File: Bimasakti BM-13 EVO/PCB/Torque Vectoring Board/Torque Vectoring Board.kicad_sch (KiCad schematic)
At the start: 24 parts, among them J1 +5, J2 Can ESC 1, J3 Can ESC 2, J4 APPS, J5 +12, J6 Steering Angle, J7 GPOS, U3 SN65HVD230, U4 SN65HVD230, U5 ADS1115IDGS

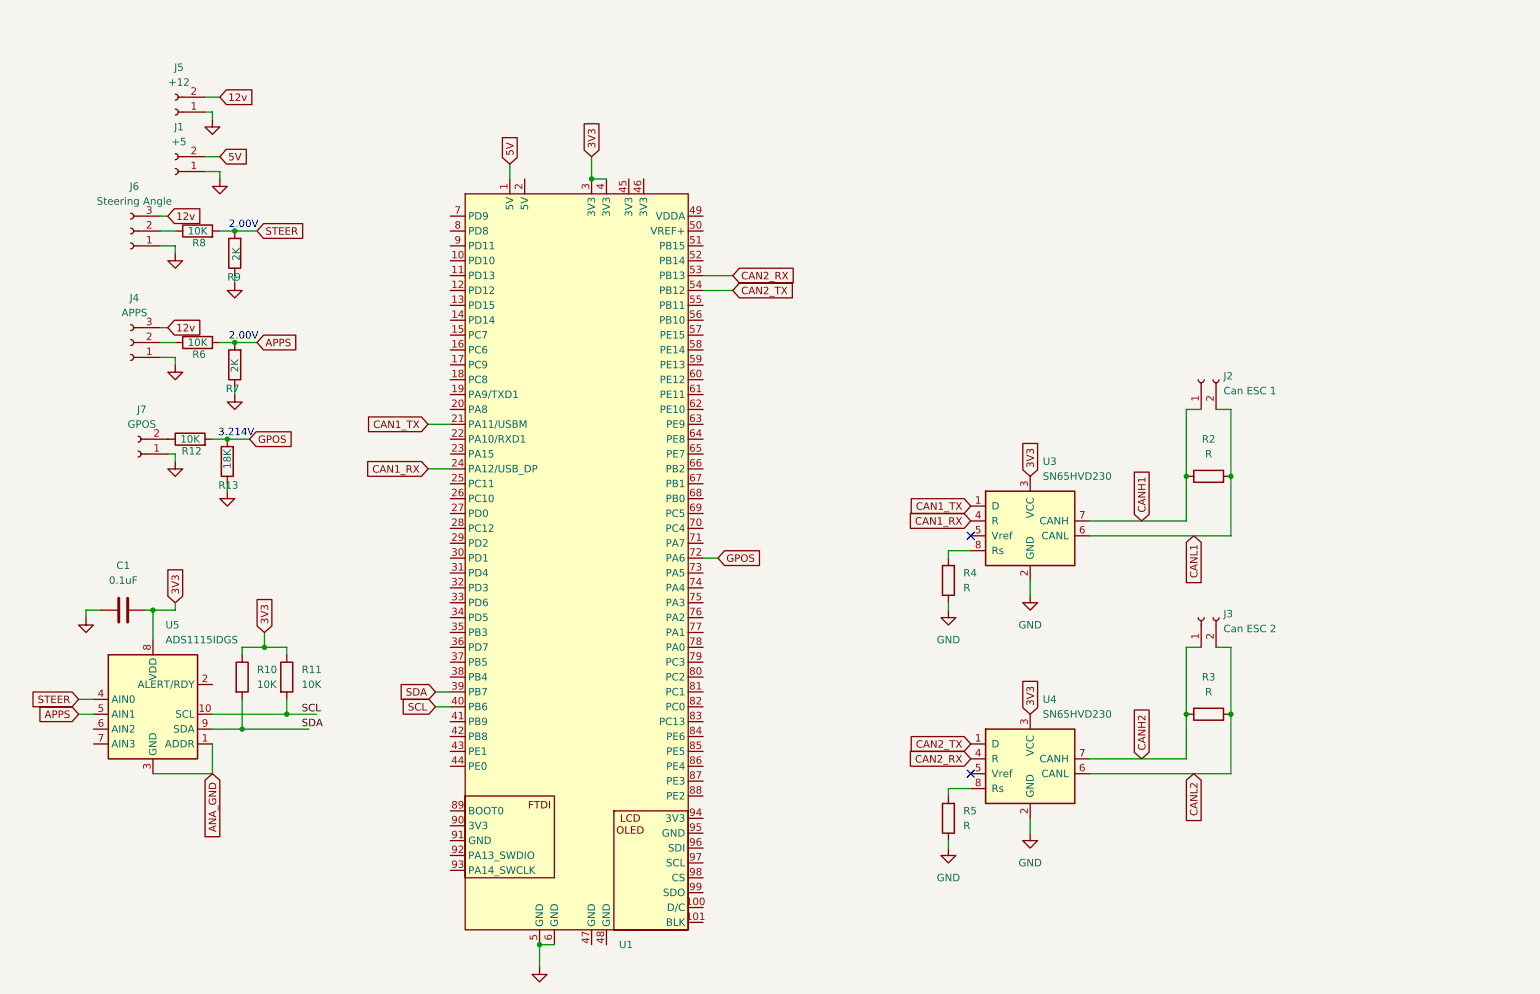
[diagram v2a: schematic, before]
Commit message: tv board kurang IMU
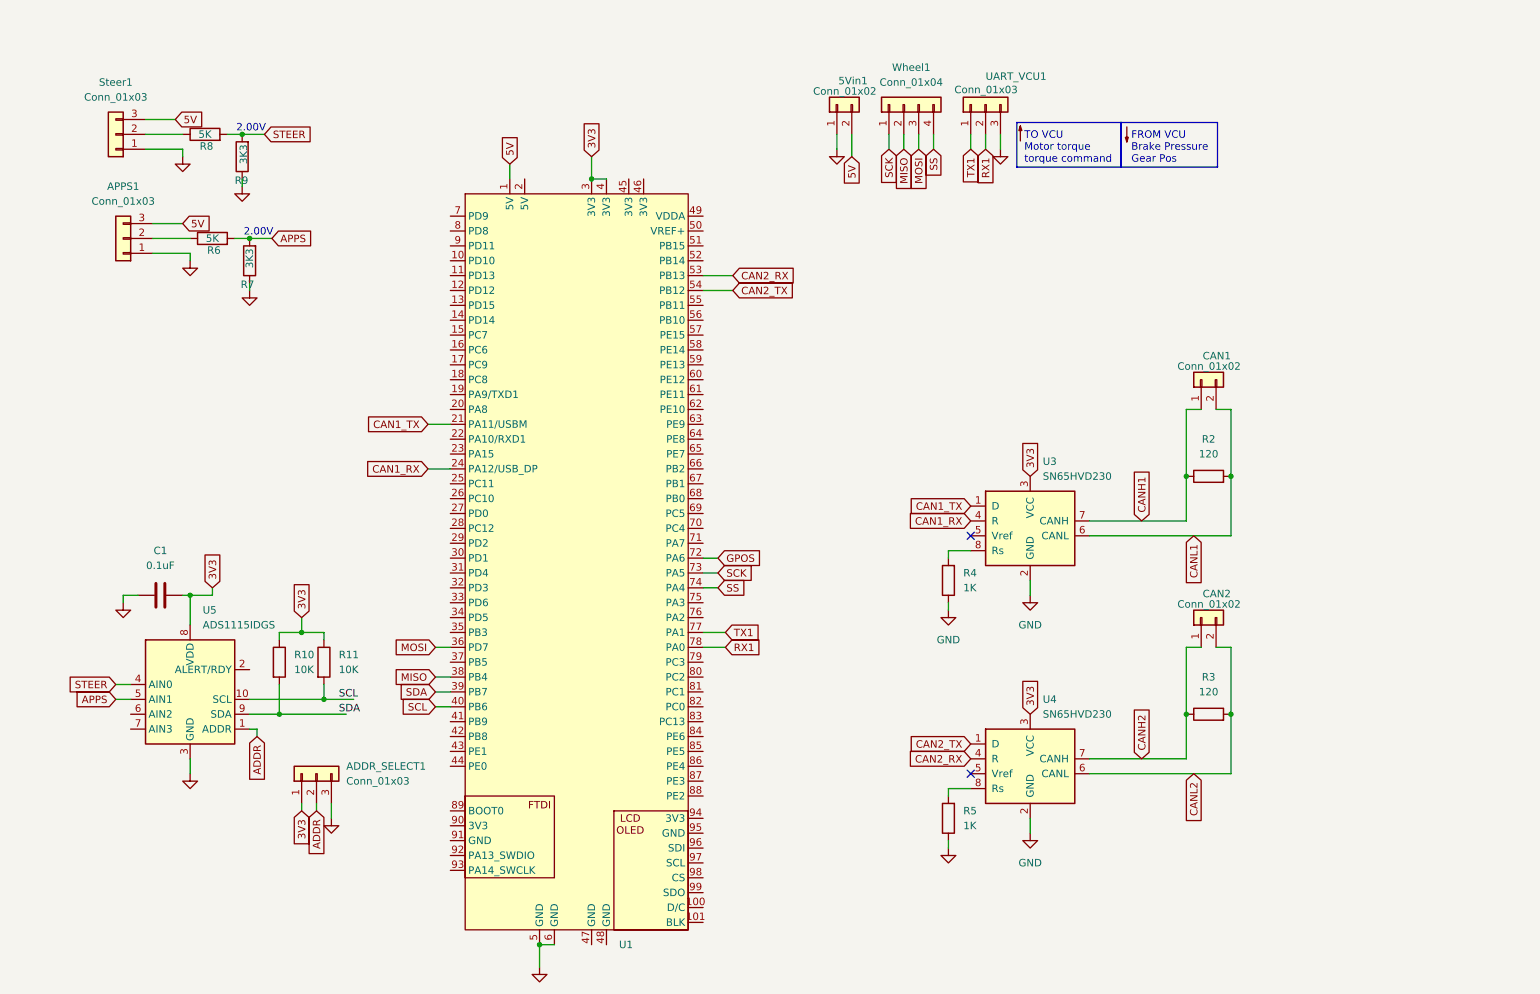
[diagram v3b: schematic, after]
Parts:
- removed J1: +5, Connector_JST:JST_EH_B2B-EH-A_1x02_P2.50mm_Vertical, symbol Connector:Conn_01x02_Socket
- removed J2: Can ESC 1, Connector_JST:JST_EH_B2B-EH-A_1x02_P2.50mm_Vertical, symbol Connector:Conn_01x02_Socket
- removed J3: Can ESC 2, Connector_JST:JST_EH_B2B-EH-A_1x02_P2.50mm_Vertical, symbol Connector:Conn_01x02_Socket
- removed J4: APPS, symbol Connector:Conn_01x03_Socket
- removed J5: +12, Connector_JST:JST_EH_B2B-EH-A_1x02_P2.50mm_Vertical, symbol Connector:Conn_01x02_Socket
- removed J6: Steering Angle, symbol Connector:Conn_01x03_Socket
- removed J7: GPOS, symbol Connector:Conn_01x02_Socket
- removed R12: 10K, Resistor_SMD:R_0805_2012Metric, symbol Device:R
- removed R13: 18K, Resistor_SMD:R_0805_2012Metric, symbol Device:R
- added 5Vin1, CAN1, CAN2: Conn_01x02, Connector_JST:JST_XH_B2B-XH-A_1x02_P2.50mm_Vertical, symbol Connector_Generic:Conn_01x02
- added ADDR_SELECT1: Conn_01x03, Connector_PinHeader_2.54mm:PinHeader_1x03_P2.54mm_Vertical, symbol Connector_Generic:Conn_01x03
- added APPS1, Steer1, UART_VCU1: Conn_01x03, Connector_JST:JST_XH_B3B-XH-A_1x03_P2.50mm_Vertical, symbol Connector_Generic:Conn_01x03
- added Wheel1: Conn_01x04, Connector_JST:JST_XH_B4B-XH-A_1x04_P2.50mm_Vertical, symbol Connector_Generic:Conn_01x04
- R2, R3: value R -> 120
- R4, R5: value R -> 1K
- R6, R8: value 10K -> 5K
- R7, R9: value 2K -> 3K3
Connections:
- net 3V3: now also ADDR_SELECT1.1 (Pin_1)
- net 5V: now also 5Vin1.2 (Pin_2), APPS1.3 (Pin_3), Steer1.3 (Pin_3)
- net CANH1: now also CAN1.1 (Pin_1)
- net CANH2: now also CAN2.1 (Pin_1)
- net CANL1: now also CAN1.2 (Pin_2)
- net CANL2: now also CAN2.2 (Pin_2)
- net GND: now also U5.3 (GND), 5Vin1.1 (Pin_1), ADDR_SELECT1.3 (Pin_3), APPS1.1 (Pin_1), Steer1.1 (Pin_1), UART_VCU1.3 (Pin_3)
- net at R8.1: now also Steer1.2 (Pin_2)
- net at R6.1: now also APPS1.2 (Pin_2)
- net MOSI: now reaches U1.36 (PD7)
- net MOSI: now also Wheel1.3 (Pin_3)
- net MISO: now reaches U1.38 (PB4)
- net MISO: now also Wheel1.2 (Pin_2)
- net SCK: now reaches U1.73 (PA5)
- net SCK: now also Wheel1.1 (Pin_1)
- net SS: now reaches U1.74 (PA4)
- net SS: now also Wheel1.4 (Pin_4)
- net TX1: now reaches U1.77 (PA1)
- net TX1: now also UART_VCU1.1 (Pin_1)
- net RX1: now reaches U1.78 (PA0)
- net RX1: now also UART_VCU1.2 (Pin_2)
- net ANA_GND renamed ADDR
- net ADDR: now also ADDR_SELECT1.2 (Pin_2); no longer U5.3 (GND)
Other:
- note added: "FROM VCU Brake Pressure Gear Pos"
- note added: "TO VCU Motor torque torque command"
- note removed: "3.214V"
- moved on the sheet: C1, R10, R11, R6, R7, R8, R9, U5

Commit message: cicil assembly
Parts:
- added H1, H2, H3, H4: MountingHole_Pad, MountingHole:MountingHole_3.2mm_M3_ISO7380_Pad_TopBottom, symbol Mechanical:MountingHole_Pad
- added R12, R13: 10K, Resistor_SMD:R_0805_2012Metric, symbol Device:R
- added U2: ~, 0_bno055:0_BNO055, symbol 0_BNO055:bno055
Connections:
- net 3V3: now also R12.1, R13.1, U2.1 (VCC)
- net GND: now also H1.1, H2.1, H3.1, H4.1, U2.2 (GND)
- net SCL: now also R12.2, U2.3 (SCL)
- net SDA: now also R13.2, U2.4 (SDA)

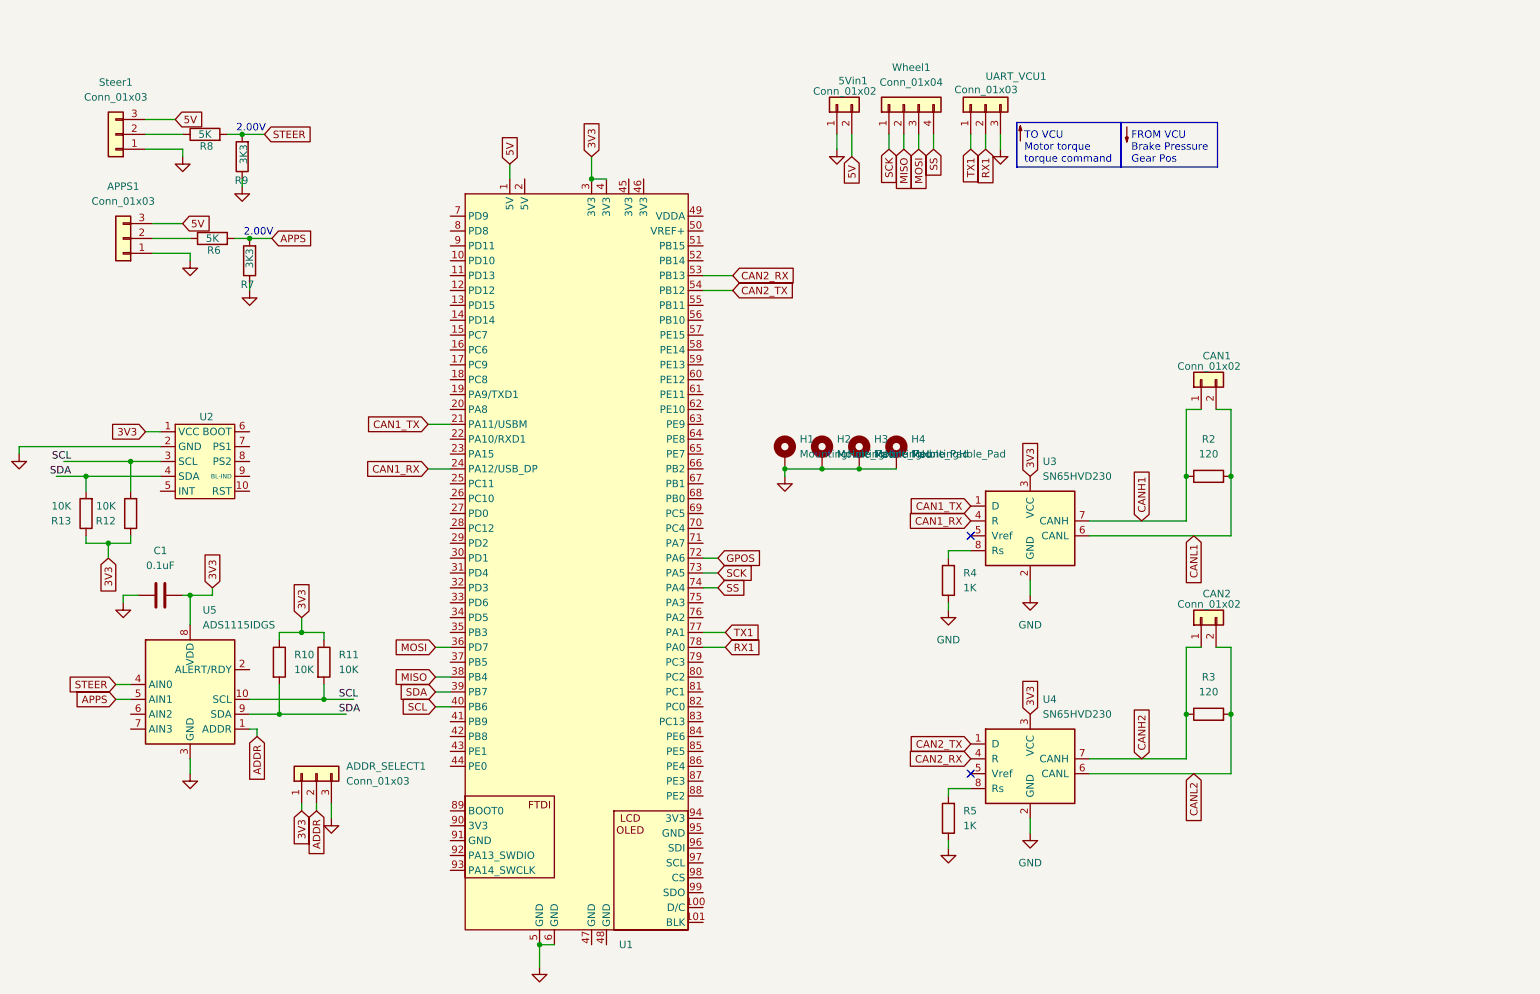
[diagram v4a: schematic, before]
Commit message: pdm selesai ril, tv board sudah bagus kurang cek (mungkin ganti konektor)
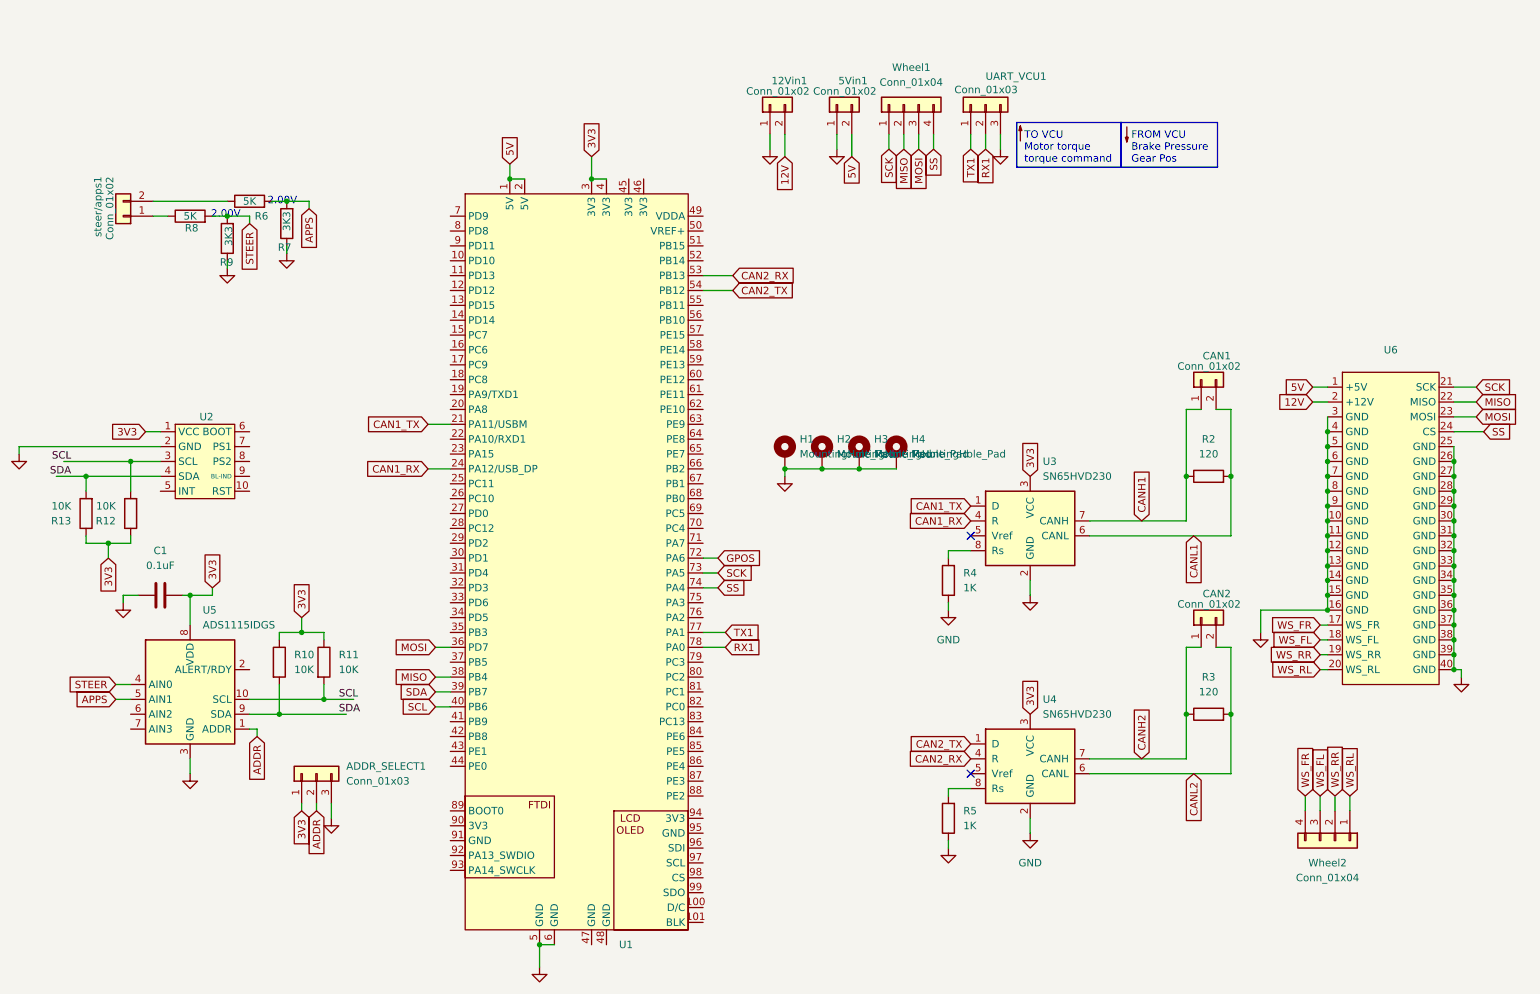
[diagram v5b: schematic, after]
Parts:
- removed APPS1, Steer1: Conn_01x03, Connector_JST:JST_XH_B3B-XH-A_1x03_P2.50mm_Vertical, symbol Connector_Generic:Conn_01x03
- added 12Vin1, steer/apps1: Conn_01x02, Connector_JST:JST_XH_B2B-XH-A_1x02_P2.50mm_Vertical, symbol Connector_Generic:Conn_01x02
- added U6: ~, 0_CUSTOM_PCB:wheelspeed, symbol 0_CUSTOM_PCB:Wheelspeed
- added Wheel2: Conn_01x04, Connector_JST:JST_XH_B4B-XH-A_1x04_P2.50mm_Vertical, symbol Connector_Generic:Conn_01x04
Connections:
- net 5V: now also U1.2 (5V), U6.1 (+5V)
- net GND: now also 12Vin1.1 (Pin_1), U6.10 (GND), U6.11 (GND), U6.12 (GND), U6.13 (GND), U6.14 (GND), U6.15 (GND), U6.16 (GND), U6.25 (GND), U6.26 (GND), U6.27 (GND), U6.28 (GND), U6.29 (GND), U6.3 (GND), U6.30 (GND), U6.31 (GND), U6.32 (GND), U6.33 (GND), U6.34 (GND), U6.35 (GND), U6.36 (GND), U6.37 (GND), U6.38 (GND), U6.39 (GND), U6.4 (GND), U6.40 (GND), U6.5 (GND), U6.6 (GND), U6.7 (GND), U6.8 (GND), U6.9 (GND)
- net MISO: now also U6.22 (MISO)
- net MOSI: now also U6.23 (MOSI)
- net SCK: now also U6.21 (SCK)
- net SS: now also U6.24 (CS)
- net at R8.1: now also steer/apps1.1 (Pin_1)
- net at R6.1: now also steer/apps1.2 (Pin_2)
- new net 12V: 12Vin1.2 (Pin_2), U6.2 (+12V)
- new net WS_FL: U6.18 (WS_FL), Wheel2.3 (Pin_3)
- new net WS_FR: U6.17 (WS_FR), Wheel2.4 (Pin_4)
- new net WS_RL: U6.20 (WS_RL), Wheel2.1 (Pin_1)
- new net WS_RR: U6.19 (WS_RR), Wheel2.2 (Pin_2)
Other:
- moved on the sheet: R6, R7, R8, R9

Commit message: buat placeholder baru dan ganti konektor
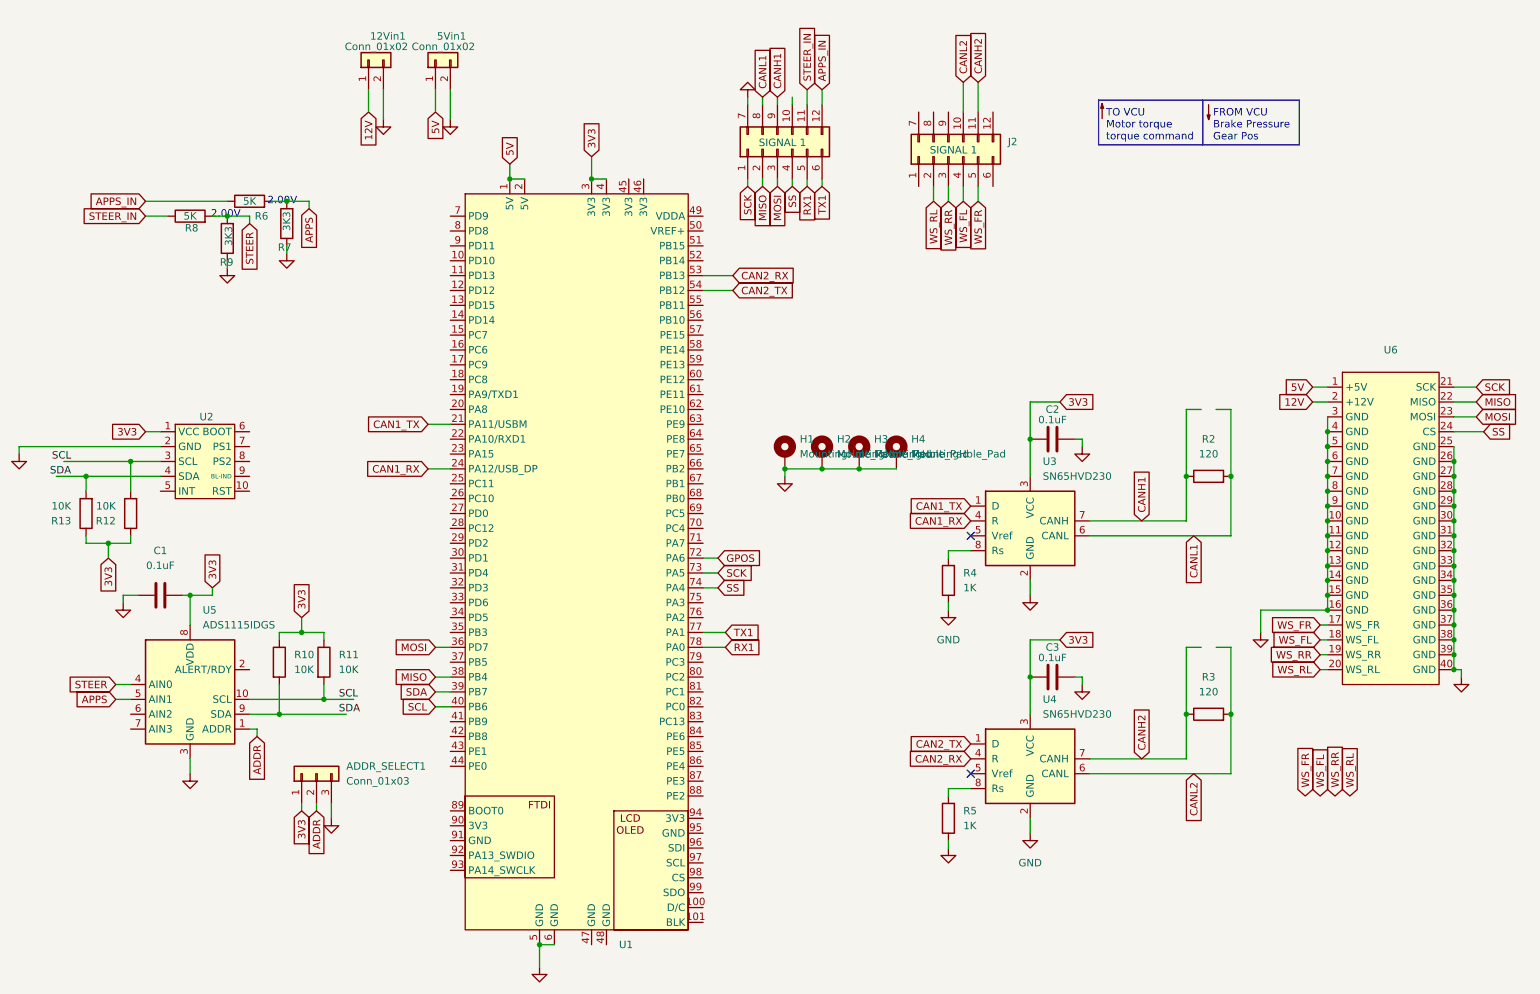
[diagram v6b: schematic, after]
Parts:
- removed CAN1, CAN2, steer/apps1: Conn_01x02, Connector_JST:JST_XH_B2B-XH-A_1x02_P2.50mm_Vertical, symbol Connector_Generic:Conn_01x02
- removed UART_VCU1: Conn_01x03, Connector_JST:JST_XH_B3B-XH-A_1x03_P2.50mm_Vertical, symbol Connector_Generic:Conn_01x03
- removed Wheel1, Wheel2: Conn_01x04, Connector_JST:JST_XH_B4B-XH-A_1x04_P2.50mm_Vertical, symbol Connector_Generic:Conn_01x04
- added C2, C3: 0.1uF, Capacitor_SMD:C_0603_1608Metric, symbol Device:C
- added J1, J2: SIGNAL 1, Connector_Molex:Molex_Nano-Fit_105310-xx12_2x06_P2.50mm_Vertical, symbol Connector_Generic:Conn_02x06_Top_Bottom
- 12Vin1, 5Vin1: footprint Connector_JST:JST_XH_B2B-XH-A_1x02_P2.50mm_Vertical -> Connector_Molex:Molex_Nano-Fit_105309-xx02_1x02_P2.50mm_Vertical
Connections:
- net 12V: now also 12Vin1.1 (Pin_1); no longer 12Vin1.2 (Pin_2)
- net 3V3: now also C2.1, C3.1
- net 5V: now also 5Vin1.1 (Pin_1); no longer 5Vin1.2 (Pin_2)
- net CANH1: now also J1.9 (Pin_9)
- net CANH2: now also J2.11 (Pin_11)
- net CANL1: now also J1.8 (Pin_8)
- net CANL2: now also J2.10 (Pin_10)
- net GND: now also 12Vin1.2 (Pin_2), 5Vin1.2 (Pin_2), C2.2, C3.2, J1.7 (Pin_7); no longer 12Vin1.1 (Pin_1), 5Vin1.1 (Pin_1)
- net MISO: now also J1.2 (Pin_2)
- net MOSI: now also J1.3 (Pin_3)
- net RX1: now also J1.5 (Pin_5)
- net SCK: now also J1.1 (Pin_1)
- net SS: now also J1.4 (Pin_4)
- net TX1: now also J1.6 (Pin_6)
- net WS_FL: now also J2.4 (Pin_4)
- net WS_FR: now also J2.5 (Pin_5)
- net WS_RL: now also J2.2 (Pin_2)
- net WS_RR: now also J2.3 (Pin_3)
- net STEER_IN: now reaches R8.1
- net STEER_IN: now also J1.11 (Pin_11)
- net APPS_IN: now reaches R6.1
- net APPS_IN: now also J1.12 (Pin_12)
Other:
- moved on the sheet: 12Vin1, 5Vin1

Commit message: assembly kurang pneumatic, kurang wiring dudukan motherboard
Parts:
- added R14: 5K, Resistor_SMD:R_0805_2012Metric, symbol Device:R
- added R15: 3K3, Resistor_SMD:R_0805_2012Metric, symbol Device:R
- J2: value SIGNAL 1 -> SIGNAL 2
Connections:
- net GND: now also R15.1
- net STEER_IN: now also J1.10 (Pin_10); no longer J1.11 (Pin_11)
- net APPS1: now reaches U5.6 (AIN2)
- net APPS1: now also R14.2, R15.2
- net APPS renamed APPS2
- net APPS_IN renamed APPS_IN1
- net APPS_IN1: now also R14.1; no longer R6.1
- net CANH1 renamed ESC1_HI
- net CANH2 renamed ESC2_HI
- net CANL1 renamed ESC1_LO
- net CANL2 renamed ESC2_LO
- net RX1 renamed STM_TX
- net TX1 renamed STM_RX
- new net APPS_IN2: J1.11 (Pin_11), R6.1
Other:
- moved on the sheet: R8, R9
